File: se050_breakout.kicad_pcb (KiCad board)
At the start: 2 copper layers, 16.3 x 12.7 mm, 9 parts, among them J1 Conn_01x05_Pin

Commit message: Add JP1 solder jumper to tie ENA high without a spare GPIO
The SE050 comes up in deep power-down because R3 holds ENA low, so a
host that never drives that pin finds nothing at 0x48 - and firmware
commonly does ignore it, the Meshtastic SE050 driver among others.

JP1 is a bottom-side solder jumper between ENA and 3V3, shipped open:
bridge it and the part is permanently enabled, leave it open and drive
ENA from the header as before. Closing it costs only deep power-down
(<5 uA), the one mode that pad controls; software power-down with state
retention still works either way.

Gerbers regenerated from the updated board. The jumper lands on B.Cu,
B.Mask and B.Silkscreen but deliberately not on B.Paste - KiCad's solder
jumper footprints carry no paste aperture, so a stencil will not bridge
it by accident.

DRC on the updated board: 0 violations, 0 unconnected, 0 schematic
parity issues.
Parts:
- added JP1: ENA, Jumper:SolderJumper-2_P1.3mm_Open_RoundedPad1.0x1.5mm, B.Cu at (117.1, 81.6)
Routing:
- net SE050_ENA: track 7.73 -> 10.5 mm
- net +3.3V: track 18.7 -> 21.5 mm
- net GND: vias 30 -> 28

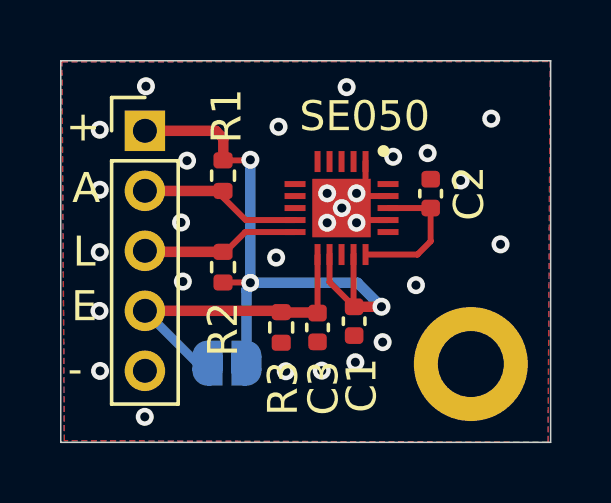
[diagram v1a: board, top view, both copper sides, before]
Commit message: Tie SE050 RST_N to ground instead of the 3V3 rail
Pin 14 is referenced to VCC, and VCC reaches the die from VOUT through
an internal switch that opens in deep power-down. Since R3 holds ENA low
by default, deep power-down is this board's resting state: VCC sits at
0 V while VIN stays at 3.3 V, leaving a pin tied to the rail above its
own reference.

The data sheet allows either VCC or VSS for this pad, and VSS is the one
that holds in every state. It cannot hold the part in reset either,
because RST_N is only active when the ISO7816 interface is enabled,
which is not the case on generic E2 parts.

Gerbers regenerated. DRC: 0 violations, 0 unconnected, 0 schematic
parity issues.
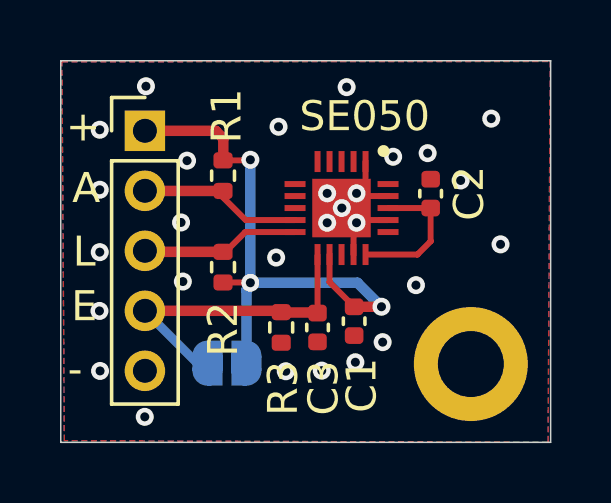
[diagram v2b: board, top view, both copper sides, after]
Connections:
- SE050 pad 14: +3.3V -> GND
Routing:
- net +3.3V: track 21.5 -> 19.8 mm
- net GND: track 6.44 -> 7.55 mm
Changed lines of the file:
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@@
 			(size 0.2 0.7)
 			(layers "F.Cu" "F.Mask" "F.Paste")
-			(net "+3.3V")
+			(net "GND")
 			(pinfunction "ISO_7816_RST_N_14")
 			(pintype "passive")
@@
 	)
 	(segment
-		(start 121.35 78)
-		(end 121.35 79.72)
-		(width 0.2)
-		(layer "F.Cu")
-		(net "+3.3V")
-	)
-	(segment
 		(start 117.89 74.86)
 		(end 117.91 74.84)
@@
 		(width 0.2)
 		(layer "F.Cu")
+		(net "GND")
+	)
+	(segment
+		(start 121.35 77.04)
+		(end 121.45 76.94)
+		(width 0.2)
+		(layer "F.Cu")
+		(net "GND")
+	)
+	(segment
+		(start 121.35 78)
+		(end 121.35 77.04)
+		(width 0.2)
+		(layer "F.Cu")
